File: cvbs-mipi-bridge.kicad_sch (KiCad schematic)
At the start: 105 parts, among them IC1 ADV7280BCPZ-M, IC2 TLV70018, IC4 SN74AUP1G17DCKR, IC5 SN74AUP1G17DCKR, J1 WE_68715014522, J2 61300211121, J7 61300211121, Q1 BSS138APW, Q2 BSS138APW, Q3 BSS138APW, Q4 BSS138APW, Y1 ABM8G-28.63636MHZ-18-D2Y-T

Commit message: Cleanup
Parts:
- removed C12: C_1u_0603, antmicro-cvbs-mipi-bridge-footprints:0603-cap, symbol antmicro-cvbs-mipi-bridge:C_1u_0603
- added C12: C_1u_0603, cvbs-mipi-bridge-footprints:0603-cap, symbol cvbs-mipi-bridge:C_1u_0603
- AIN1, AIN2, AIN3, AIN4: footprint antmicro-cvbs-mipi-bridge-footprints:PJRAN1X1U01X -> cvbs-mipi-bridge-footprints:PJRAN1X1U01X; symbol antmicro-cvbs-mipi-bridge:PJRAN1X1U01X -> cvbs-mipi-bridge:PJRAN1X1U01X
- C1, C10, C13, C14, C16, C17, C2, C20, C21, C24, C26, C3, C4, C5, C6, C7: footprint antmicro-cvbs-mipi-bridge-footprints:0402-cap -> cvbs-mipi-bridge-footprints:0402-cap; symbol antmicro-cvbs-mipi-bridge:C_100n_0402 -> cvbs-mipi-bridge:C_100n_0402
- C11, C15, C18, C19: footprint antmicro-cvbs-mipi-bridge-footprints:0402-cap -> cvbs-mipi-bridge-footprints:0402-cap; symbol antmicro-cvbs-mipi-bridge:C_10n_0402 -> cvbs-mipi-bridge:C_10n_0402
- C22, C23: footprint antmicro-cvbs-mipi-bridge-footprints:0402-cap -> cvbs-mipi-bridge-footprints:0402-cap; symbol antmicro-cvbs-mipi-bridge:C_10p_0402 -> cvbs-mipi-bridge:C_10p_0402
- C27, C28, C8, C9: footprint antmicro-cvbs-mipi-bridge-footprints:0402-cap -> cvbs-mipi-bridge-footprints:0402-cap; symbol antmicro-cvbs-mipi-bridge:C_1u_0402 -> cvbs-mipi-bridge:C_1u_0402
- D1, D2, D3, D4: footprint antmicro-cvbs-mipi-bridge-footprints:SOT-23-3 -> cvbs-mipi-bridge-footprints:SOT-23-3; symbol antmicro-cvbs-mipi-bridge:PESD1CAN_215 -> cvbs-mipi-bridge:PESD1CAN_215
- D5, D6, D7, D8: footprint antmicro-cvbs-mipi-bridge-footprints:LED_0603 -> cvbs-mipi-bridge-footprints:LED_0603; symbol antmicro-cvbs-mipi-bridge:KP-1608ZGC -> cvbs-mipi-bridge:KP-1608ZGC
- FB1, FB3, FB4, FB5: footprint antmicro-cvbs-mipi-bridge-footprints:0805-res -> cvbs-mipi-bridge-footprints:0805-res; symbol antmicro-cvbs-mipi-bridge:742792022 -> cvbs-mipi-bridge:742792022
- IC1: footprint antmicro-cvbs-mipi-bridge-footprints:LFCSP-32-1EP-5x5mm -> cvbs-mipi-bridge-footprints:LFCSP-32-1EP-5x5mm; symbol antmicro-cvbs-mipi-bridge:ADV7280BCPZ-M -> cvbs-mipi-bridge:ADV7280BCPZ-M
- IC2: footprint antmicro-cvbs-mipi-bridge-footprints:SC-70-5 -> cvbs-mipi-bridge-footprints:SC-70-5; symbol antmicro-cvbs-mipi-bridge:TLV70018 -> cvbs-mipi-bridge:TLV70018
- IC4, IC5: footprint antmicro-cvbs-mipi-bridge-footprints:SOT-753 -> cvbs-mipi-bridge-footprints:SOT-753; symbol antmicro-cvbs-mipi-bridge:SN74AUP1G17DCKR -> cvbs-mipi-bridge:SN74AUP1G17DCKR
- J1: footprint antmicro-cvbs-mipi-bridge-footprints:WE_68715014522 -> cvbs-mipi-bridge-footprints:WE_68715014522; symbol antmicro-cvbs-mipi-bridge:WE_68715014522 -> cvbs-mipi-bridge:WE_68715014522
- J2, J7: footprint antmicro-cvbs-mipi-bridge-footprints:PinHeader_1x2_P2.54_Drill0.9mm -> cvbs-mipi-bridge-footprints:PinHeader_1x2_P2.54_Drill0.9mm; symbol antmicro-cvbs-mipi-bridge:61300211121 -> cvbs-mipi-bridge:61300211121
- MP1, MP2, MP3, MP4: footprint antmicro-cvbs-mipi-bridge-footprints:9774030243R -> cvbs-mipi-bridge-footprints:9774030243R; symbol antmicro-cvbs-mipi-bridge:9774030243R -> cvbs-mipi-bridge:9774030243R
- N1: footprint antmicro-cvbs-mipi-bridge-footprints:antmicro-logo_scaled_20mm -> cvbs-mipi-bridge-footprints:antmicro-logo_scaled_20mm; symbol antmicro-cvbs-mipi-bridge:antmicro_logo -> cvbs-mipi-bridge:antmicro_logo
- N2: footprint antmicro-cvbs-mipi-bridge-footprints:oshw-logo -> cvbs-mipi-bridge-footprints:oshw-logo; symbol antmicro-cvbs-mipi-bridge:oshw_logo -> cvbs-mipi-bridge:oshw_logo
- Q1, Q2, Q3, Q4: footprint antmicro-cvbs-mipi-bridge-footprints:SC70-3 -> cvbs-mipi-bridge-footprints:SC70-3; symbol antmicro-cvbs-mipi-bridge:BSS138APW -> cvbs-mipi-bridge:BSS138APW
- R1, R10, R4, R8: footprint antmicro-cvbs-mipi-bridge-footprints:0603-res -> cvbs-mipi-bridge-footprints:0603-res; symbol antmicro-cvbs-mipi-bridge:R_24R_0603 -> cvbs-mipi-bridge:R_24R_0603
- R11, R3, R5, R9: footprint antmicro-cvbs-mipi-bridge-footprints:0402-res -> cvbs-mipi-bridge-footprints:0402-res; symbol antmicro-cvbs-mipi-bridge:R_51R_0402 -> cvbs-mipi-bridge:R_51R_0402
- R12, R13, R14, R26: footprint antmicro-cvbs-mipi-bridge-footprints:0402-res -> cvbs-mipi-bridge-footprints:0402-res; symbol antmicro-cvbs-mipi-bridge:R_470R_0402 -> cvbs-mipi-bridge:R_470R_0402
- R15: footprint antmicro-cvbs-mipi-bridge-footprints:0402-res -> cvbs-mipi-bridge-footprints:0402-res; symbol antmicro-cvbs-mipi-bridge:R_22k_0402 -> cvbs-mipi-bridge:R_22k_0402
- R16: footprint antmicro-cvbs-mipi-bridge-footprints:0402-res -> cvbs-mipi-bridge-footprints:0402-res; symbol antmicro-cvbs-mipi-bridge:R_1M0_0402 -> cvbs-mipi-bridge:R_1M0_0402
- R17, R18, R19, R27, R28, R29, R31: footprint antmicro-cvbs-mipi-bridge-footprints:0402-res -> cvbs-mipi-bridge-footprints:0402-res; symbol antmicro-cvbs-mipi-bridge:R_100k_0402 -> cvbs-mipi-bridge:R_100k_0402
- R2: footprint antmicro-cvbs-mipi-bridge-footprints:0402-res -> cvbs-mipi-bridge-footprints:0402-res; symbol antmicro-cvbs-mipi-bridge:R_1k_0402 -> cvbs-mipi-bridge:R_1k_0402
- R20, R21, R22, R23, R24, R25, R30: footprint antmicro-cvbs-mipi-bridge-footprints:0402-res -> cvbs-mipi-bridge-footprints:0402-res; symbol antmicro-cvbs-mipi-bridge:R_0R_0402 -> cvbs-mipi-bridge:R_0R_0402
- R6, R7: footprint antmicro-cvbs-mipi-bridge-footprints:0402-res -> cvbs-mipi-bridge-footprints:0402-res; symbol antmicro-cvbs-mipi-bridge:R_4k7_0402 -> cvbs-mipi-bridge:R_4k7_0402
- S1: footprint antmicro-cvbs-mipi-bridge-footprints:SW_SPST_4.2x2.8 -> cvbs-mipi-bridge-footprints:SW_SPST_4.2x2.8; symbol antmicro-cvbs-mipi-bridge:KMR2 -> cvbs-mipi-bridge:KMR2
- TP1, TP10, TP11, TP12, TP13, TP2, TP3, TP5, TP6, TP7, TP8, TP9: footprint antmicro-cvbs-mipi-bridge-footprints:TP-R-1.5 -> cvbs-mipi-bridge-footprints:TP-R-1.5; symbol antmicro-cvbs-mipi-bridge:TP -> cvbs-mipi-bridge:TP
- Y1: footprint antmicro-cvbs-mipi-bridge-footprints:KX-7 -> cvbs-mipi-bridge-footprints:KX-7; symbol antmicro-cvbs-mipi-bridge:ABM8G-28.63636MHZ-18-D2Y-T -> cvbs-mipi-bridge:ABM8G-28.63636MHZ-18-D2Y-T
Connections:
- net GND: now also C12.2
- net at FB1.2, J1.47 (Pin_47), J1.48 (Pin_48): now also C12.1

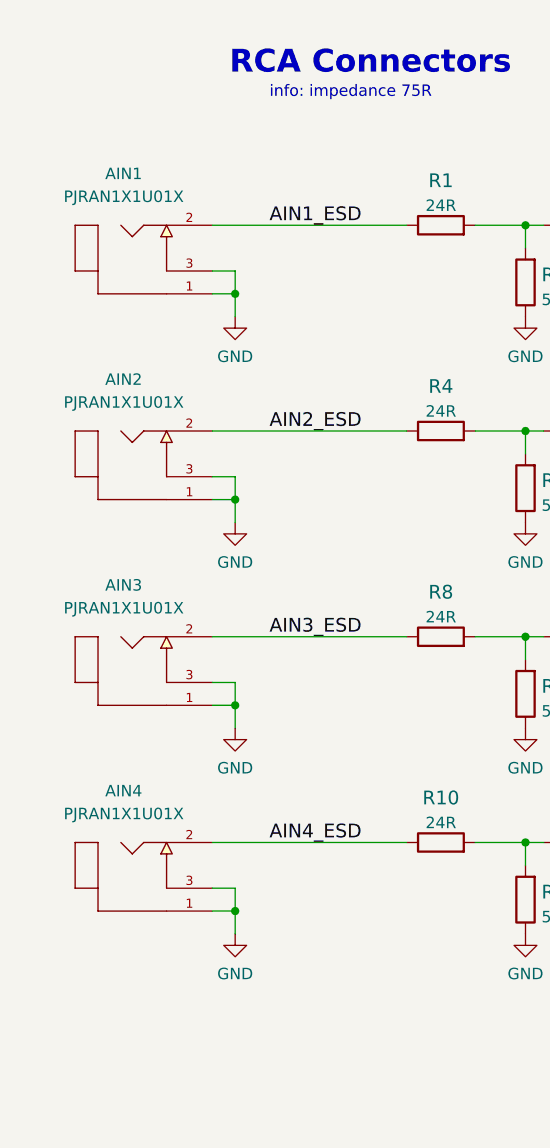
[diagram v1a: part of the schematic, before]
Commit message: Replace RCA connectors
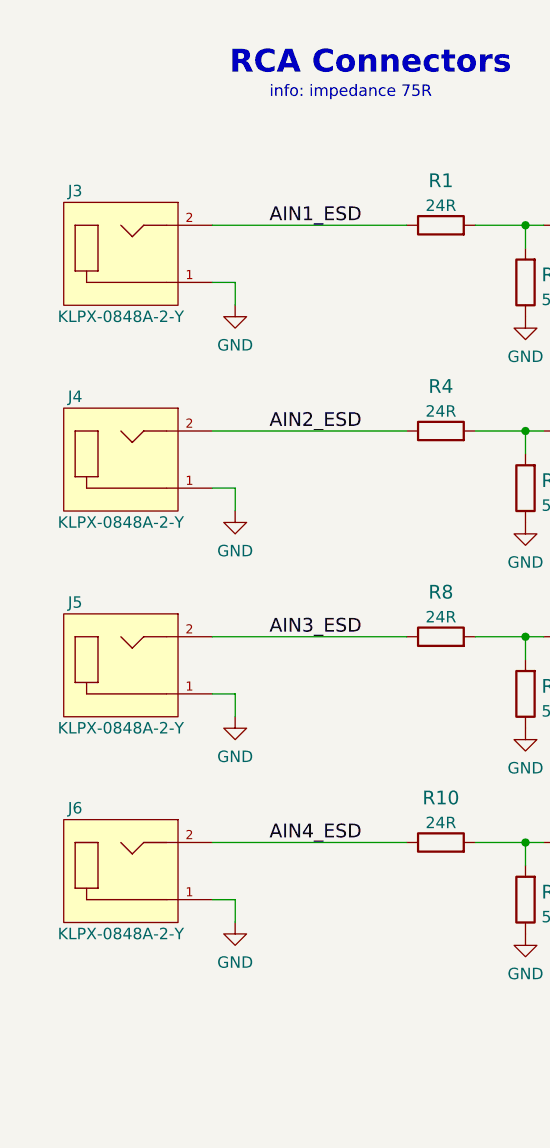
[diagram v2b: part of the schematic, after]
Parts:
- removed AIN1, AIN2, AIN3, AIN4: PJRAN1X1U01X, cvbs-mipi-bridge-footprints:PJRAN1X1U01X, symbol cvbs-mipi-bridge:PJRAN1X1U01X
- added J3, J4, J5, J6: KLPX-0848A-2-Y, cvbs-mipi-bridge-footprints:KLPX-0848A-2-Y, symbol cvbs-mipi-bridge:KLPX-0848A-2-Y
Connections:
- net AIN1_ESD: now also J3.2
- net AIN2_ESD: now also J4.2
- net AIN3_ESD: now also J5.2
- net AIN4_ESD: now also J6.2
- net GND: now also J3.1, J4.1, J5.1, J6.1

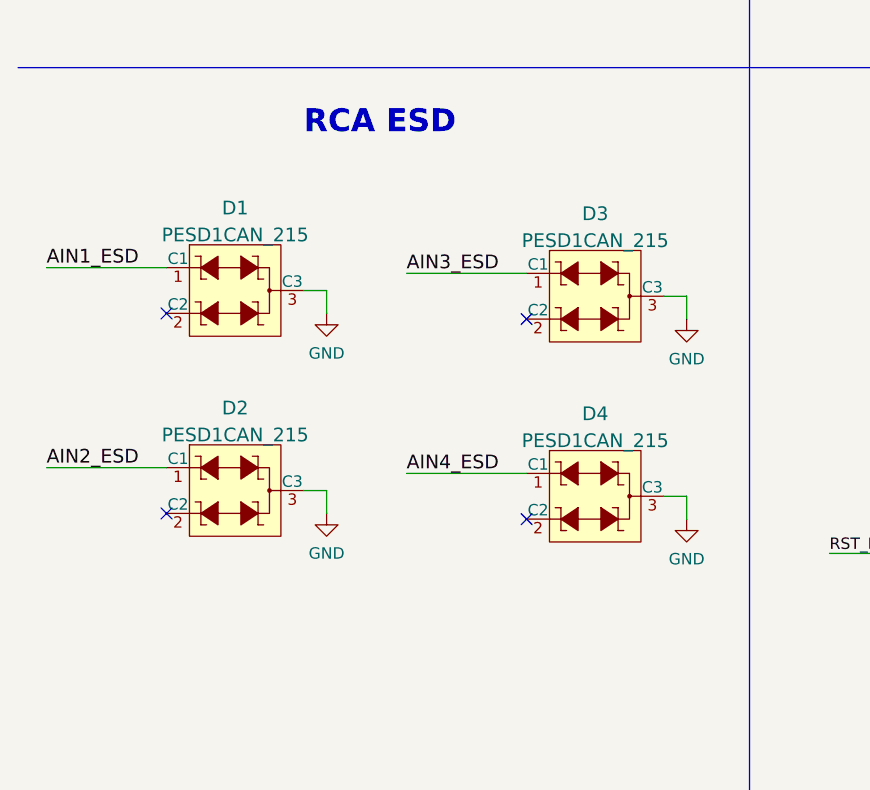
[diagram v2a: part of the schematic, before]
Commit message: Replace TVS diodes
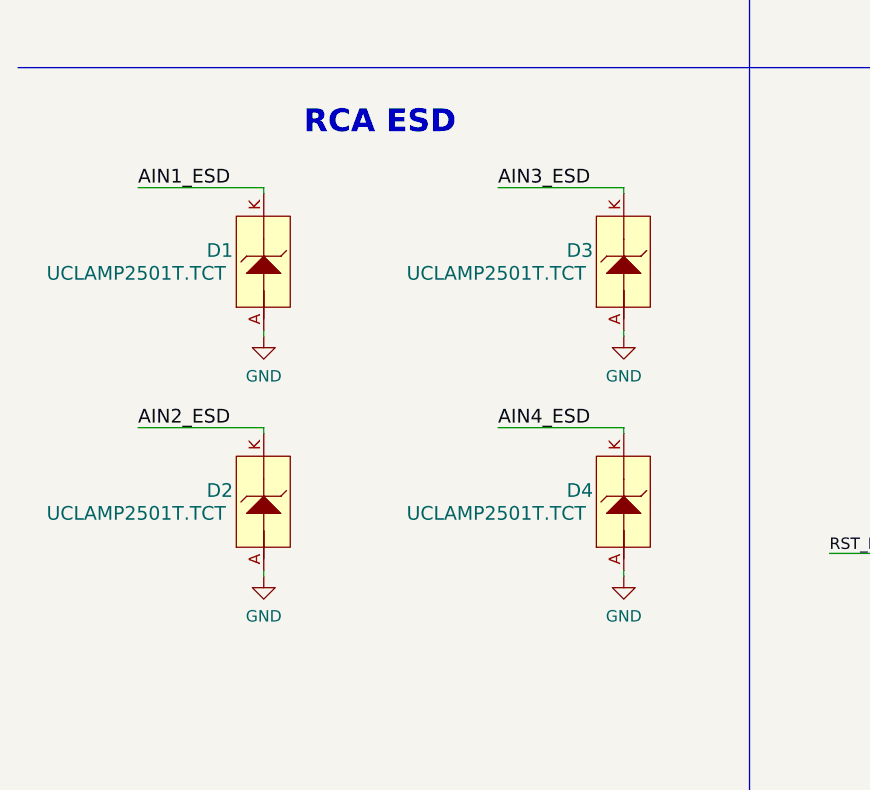
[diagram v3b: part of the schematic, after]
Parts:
- removed D1, D2, D3, D4: PESD1CAN_215, cvbs-mipi-bridge-footprints:SOT-23-3, symbol cvbs-mipi-bridge:PESD1CAN_215
- added D1, D2, D3, D4: UCLAMP2501T.TCT, cvbs-mipi-bridge-footprints:SLP1006P2T, symbol cvbs-mipi-bridge:UCLAMP2501T.TCT
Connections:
- net AIN1_ESD: now also D1.K
- net AIN2_ESD: now also D2.K
- net AIN3_ESD: now also D3.K
- net AIN4_ESD: now also D4.K
- net GND: now also D1.A, D2.A, D3.A, D4.A
- no-connect marks 43 -> 39

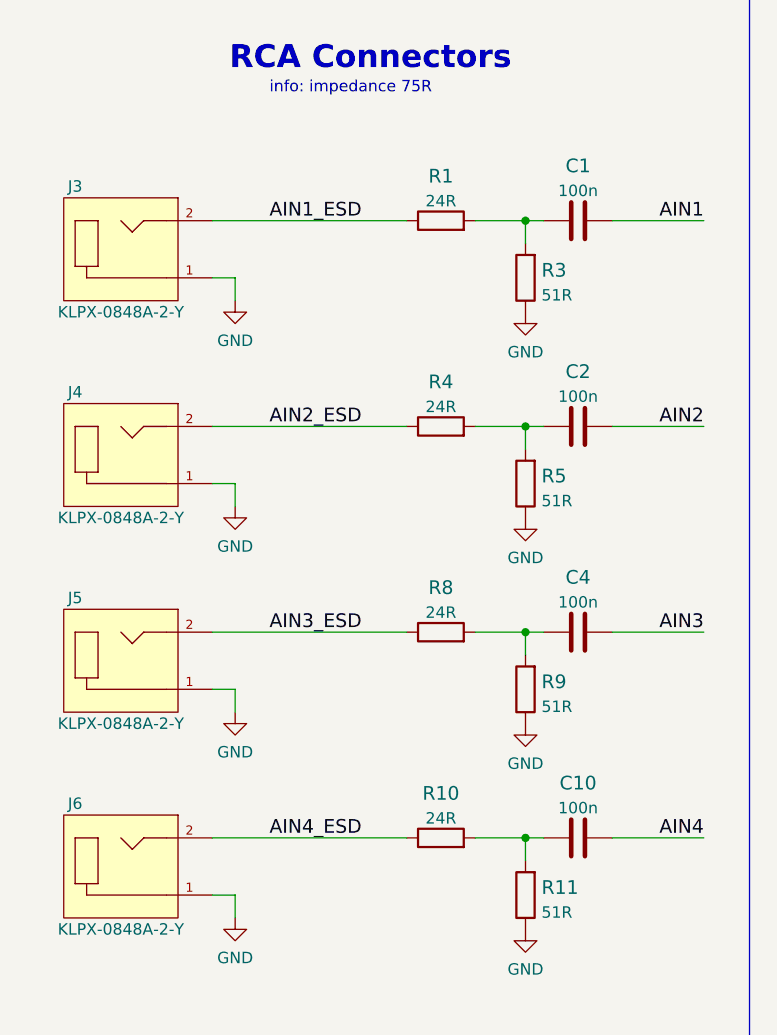
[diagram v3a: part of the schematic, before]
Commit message: Place components, route video signals
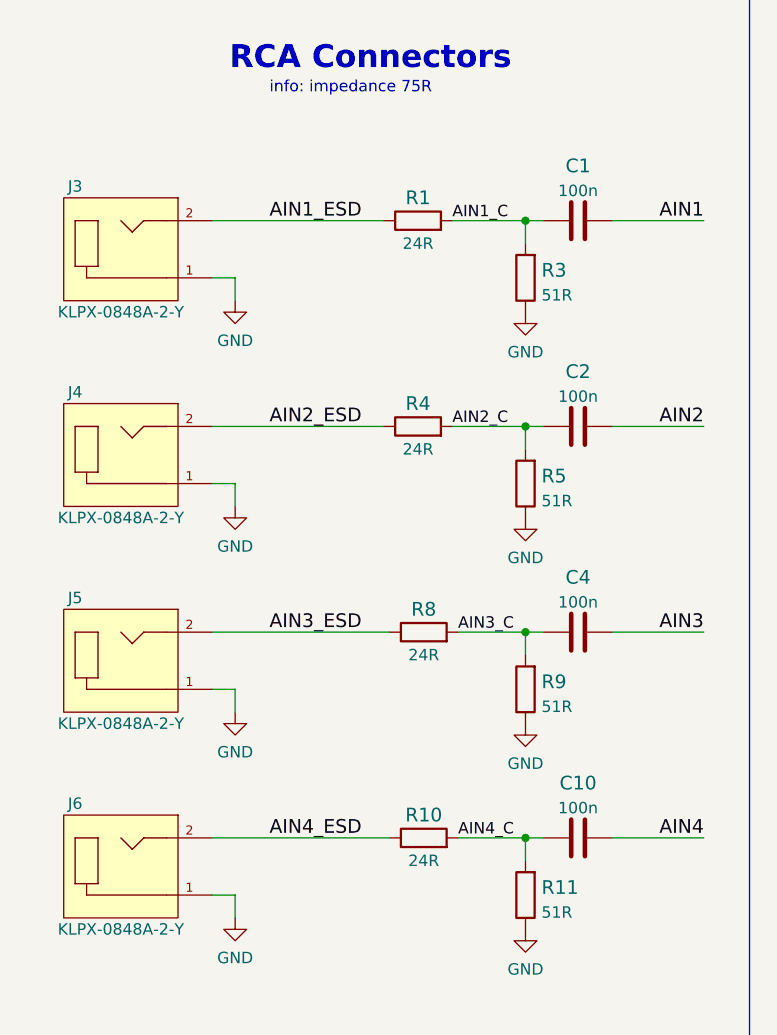
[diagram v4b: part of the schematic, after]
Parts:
- removed R1, R10, R4, R8: R_24R_0603, cvbs-mipi-bridge-footprints:0603-res, symbol cvbs-mipi-bridge:R_24R_0603
- added R1, R10, R4, R8: R_24R_0402, antmicro-footprints:0402-res, symbol antmicroResistors0402:R_24R_0402
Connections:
- net AIN1_ESD: now also R1.1
- net AIN2_ESD: now also R4.1
- net AIN3_ESD: now also R8.1
- net AIN4_ESD: now also R10.1
- net AIN4_C: now reaches C10.1, R11.2
- net AIN4_C: now also R10.2
- net AIN3_C: now reaches C4.1, R9.2
- net AIN3_C: now also R8.2
- net AIN2_C: now reaches C2.1, R5.2
- net AIN2_C: now also R4.2
- net AIN1_C: now reaches C1.1, R3.2
- net AIN1_C: now also R1.2

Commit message: Loclib
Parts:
- R1, R10, R4, R8: footprint antmicro-footprints:0402-res -> cvbs-mipi-bridge-footprints:0402-res; symbol antmicroResistors0402:R_24R_0402 -> cvbs-mipi-bridge:R_24R_0402
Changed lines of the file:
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@@
     (pin "2")
   )
-  (symbol (lib_id "antmicroResistors0402:R_24R_0402") (at 57.15 92.71 0) (unit 1)
+  (symbol (lib_id "cvbs-mipi-bridge:R_24R_0402") (at 57.15 92.71 0) (unit 1)
     (in_bom yes) (on_board yes)
     (property "Reference" "R1" (id 0) (at 57.15 90.17 0)
@@
       (effects (font (size 1.524 1.524)) hide)
     )
-    (property "Footprint" "antmicro-footprints:0402-res" (id 2) (at 62.23 87.63 0)
+    (property "Footprint" "cvbs-mipi-bridge-footprints:0402-res" (id 2) (at 62.23 87.63 0)
       (effects (font (size 1.524 1.524)) (justify left) hide)
     )
@@
     (pin "2")
   )
-  (symbol (lib_id "antmicroResistors0402:R_24R_0402") (at 57.15 115.57 0) (unit 1)
+  (symbol (lib_id "cvbs-mipi-bridge:R_24R_0402") (at 57.15 115.57 0) (unit 1)
     (in_bom yes) (on_board yes)
     (property "Reference" "R4" (id 0) (at 57.15 113.03 0)
@@
       (effects (font (size 1.524 1.524)) hide)
     )
-    (property "Footprint" "antmicro-footprints:0402-res" (id 2) (at 62.23 110.49 0)
+    (property "Footprint" "cvbs-mipi-bridge-footprints:0402-res" (id 2) (at 62.23 110.49 0)
       (effects (font (size 1.524 1.524)) (justify left) hide)
     )
@@
     (pin "2")
   )
-  (symbol (lib_id "antmicroResistors0402:R_24R_0402") (at 57.785 161.29 0) (unit 1)
+  (symbol (lib_id "cvbs-mipi-bridge:R_24R_0402") (at 57.785 161.29 0) (unit 1)
     (in_bom yes) (on_board yes)
     (property "Reference" "R10" (id 0) (at 57.785 158.75 0)
@@
       (effects (font (size 1.524 1.524)) hide)
     )
-    (property "Footprint" "antmicro-footprints:0402-res" (id 2) (at 62.865 156.21 0)
+    (property "Footprint" "cvbs-mipi-bridge-footprints:0402-res" (id 2) (at 62.865 156.21 0)
       (effects (font (size 1.524 1.524)) (justify left) hide)
     )
@@
     (pin "1")
   )
-  (symbol (lib_id "antmicroResistors0402:R_24R_0402") (at 57.785 138.43 0) (unit 1)
+  (symbol (lib_id "cvbs-mipi-bridge:R_24R_0402") (at 57.785 138.43 0) (unit 1)
     (in_bom yes) (on_board yes)
     (property "Reference" "R8" (id 0) (at 57.785 135.89 0)
@@
       (effects (font (size 1.524 1.524)) hide)
     )
-    (property "Footprint" "antmicro-footprints:0402-res" (id 2) (at 62.865 133.35 0)
+    (property "Footprint" "cvbs-mipi-bridge-footprints:0402-res" (id 2) (at 62.865 133.35 0)
       (effects (font (size 1.524 1.524)) (justify left) hide)
     )
@@
     )
     (path "/44b415ce-6f62-45ef-b8e2-efa97d049c0e"
-      (reference "R1") (unit 1) (value "R_24R_0402") (footprint "antmicro-footprints:0402-res")
+      (reference "R1") (unit 1) (value "R_24R_0402") (footprint "cvbs-mipi-bridge-footprints:0402-res")
     )
     (path "/788c15c3-f2fa-476b-9815-ee73fbacef1f"
@@
     )
     (path "/ae995d8b-8eb2-4877-a3ec-d071e1288762"
-      (reference "R4") (unit 1) (value "R_24R_0402") (footprint "antmicro-footprints:0402-res")
+      (reference "R4") (unit 1) (value "R_24R_0402") (footprint "cvbs-mipi-bridge-footprints:0402-res")
     )
     (path "/dc65378e-f7c7-4bb3-99f3-625d9703f619"
@@
     )
     (path "/e902327f-d119-4e09-b8bc-d4f42f53df24"
-      (reference "R8") (unit 1) (value "R_24R_0402") (footprint "antmicro-footprints:0402-res")
+      (reference "R8") (unit 1) (value "R_24R_0402") (footprint "cvbs-mipi-bridge-footprints:0402-res")
     )
     (path "/6a3aa5f5-7d53-427b-a701-abdbab018d9d"
@@
     )
     (path "/c8e8ee5d-39ef-42bb-91fa-6442958fff4d"
-      (reference "R10") (unit 1) (value "R_24R_0402") (footprint "antmicro-footprints:0402-res")
+      (reference "R10") (unit 1) (value "R_24R_0402") (footprint "cvbs-mipi-bridge-footprints:0402-res")
     )
     (path "/1ee32727-4a84-4934-bda1-43d82efc65d6"

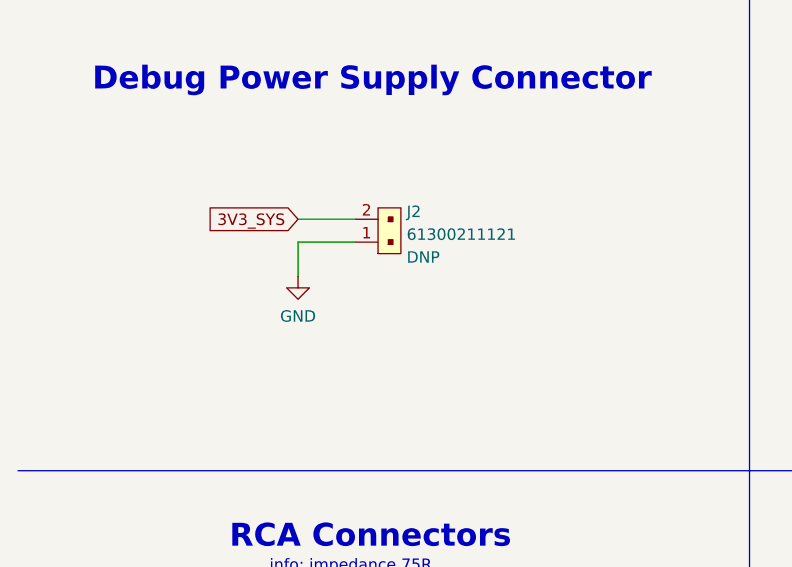
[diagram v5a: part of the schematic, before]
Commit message: Replace DC power connector
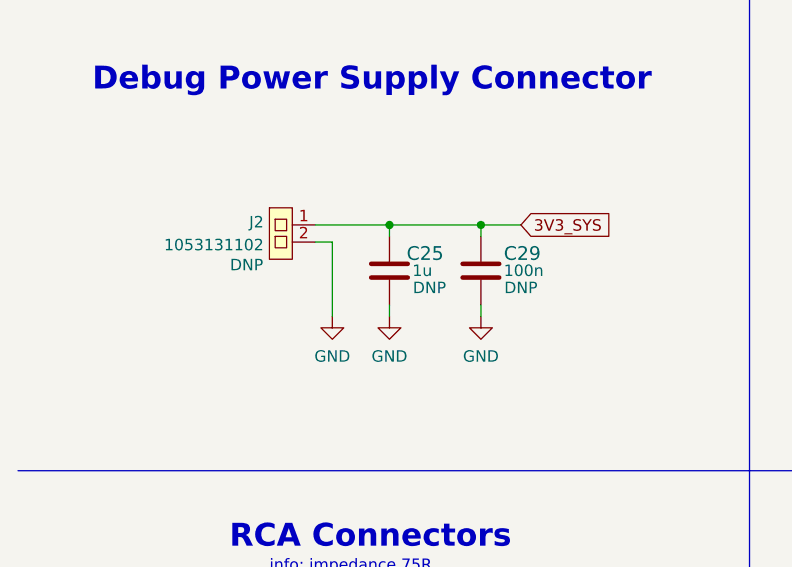
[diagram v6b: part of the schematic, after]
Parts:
- removed J2: 61300211121, cvbs-mipi-bridge-footprints:PinHeader_1x2_P2.54_Drill0.9mm, symbol cvbs-mipi-bridge:61300211121
- added C25: C_1u_0402, cvbs-mipi-bridge-footprints:0402-cap, symbol cvbs-mipi-bridge:C_1u_0402
- added C29: C_100n_0402, cvbs-mipi-bridge-footprints:0402-cap, symbol cvbs-mipi-bridge:C_100n_0402
- added J2: 1053131102, cvbs-mipi-bridge-footprints:1053131102, symbol cvbs-mipi-bridge:1053131102
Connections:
- net 3V3_SYS: now also C25.1, C29.2, J2.1
- net GND: now also C25.2, C29.1, J2.2
